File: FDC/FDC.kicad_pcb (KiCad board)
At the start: 2 copper layers, 195.4 x 115.8 mm, 60 parts, among them J1 Bus_ISA_8bit, J2 Floppy IDC, Q1 2N2219, Q2 2N3905, SW1 DSEL, U1 74LS08, U10 74LS161, U11 74LS10, U12 74LS74, U13 74LS08, U14 74LS157, U15 74LS74, U16 74LS175, U17 MC3487N, U18 74LS74, U19 74LS74, U2 74LS32, U20 74LS629, U21 74LS161, U23 74LS175, U24 74LS153, U26 74LS38, U27 74HC240, U3 74LS02, U4 74LS30, U5 74LS245, U6 uPD765BC, U7 74LS04, U8 74LS273, U9 74LS161, X1 16MHZ

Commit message: Large sync
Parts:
- moved C9 178.1 mm to (209.4, 39.1), turned to 180 degrees
- moved C5 168.4 mm to (254.1, 98.3), turned to 90 degrees
- moved C16 151.0 mm to (153.3, 43.8)
- moved C15 139.9 mm to (70.6, 43.7), turned to 270 degrees
- moved C19 136.7 mm to (147.5, 55.1)
- moved C14 126.2 mm to (123.2, 51.3)
- moved C8 119.6 mm to (212.3, 120.9), turned to 270 degrees
- moved C11 75.3 mm to (114.3, 102.4), turned to 270 degrees
- moved C6 74.7 mm to (144.2, 113.9)
- moved C10 61.2 mm to (79.6, 126.5), turned to 270 degrees
- moved C13 59.2 mm to (116.8, 119.0), turned to 90 degrees
- moved C7 55.2 mm to (128.5, 126.7), turned to 270 degrees
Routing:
- net Net-(U26-Pad12): track 10.2 -> 239.3 mm, vias 0 -> 8
- net Net-(U26-Pad10): track 10.2 -> 236.8 mm, vias 0 -> 7
- net /WE: track 53.3 -> 196.0 mm, vias 0 -> 1
- net /TCDACK: track 0.00 -> 123.6 mm, vias 0 -> 2
- net Net-(U26-Pad4): track 0.00 -> 117.5 mm, vias 0 -> 3
- net /TRK0: track 0.00 -> 117.3 mm, vias 0 -> 6
- net Net-(U1-Pad6): track 0.00 -> 80.1 mm, vias 0 -> 3
- net /DMA_GATE: track 54.9 -> 134.2 mm, vias 3 -> 6
- net Net-(U1-Pad10): track 8.67 -> 83.4 mm, vias 0 -> 2
- net +5V: track 174.2 -> 210.1 mm, vias 15 -> 23
- net /TC: track 27.2 -> 59.0 mm, vias 2 -> 1
- net Net-(U3-Pad6): track 52.8 -> 77.4 mm, vias 2 -> 3
- net GND: track 121.4 -> 142.3 mm, vias 4 -> 5
- net /PLL/8MHZ_NOM: track 81.0 -> 79.9 mm
- net Net-(Q2-Pad2): track 13.1 -> 13.8 mm

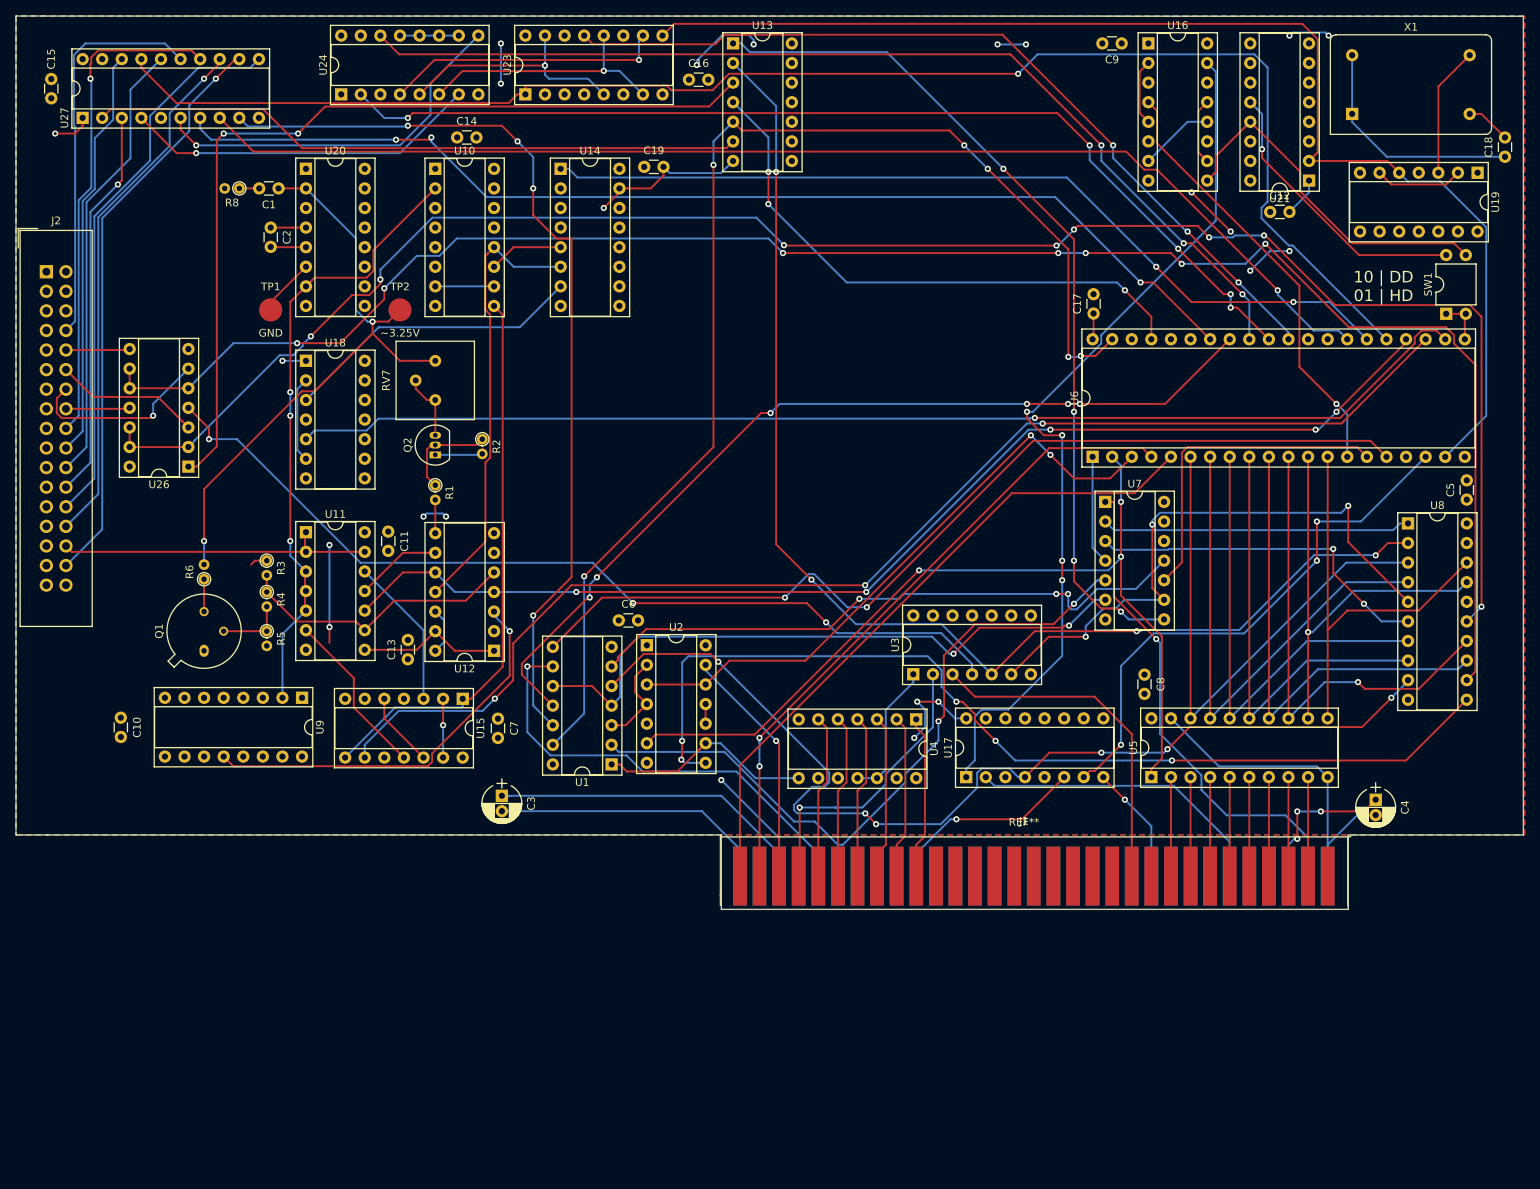
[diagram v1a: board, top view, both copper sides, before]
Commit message: Fixed missing +5V on FDC
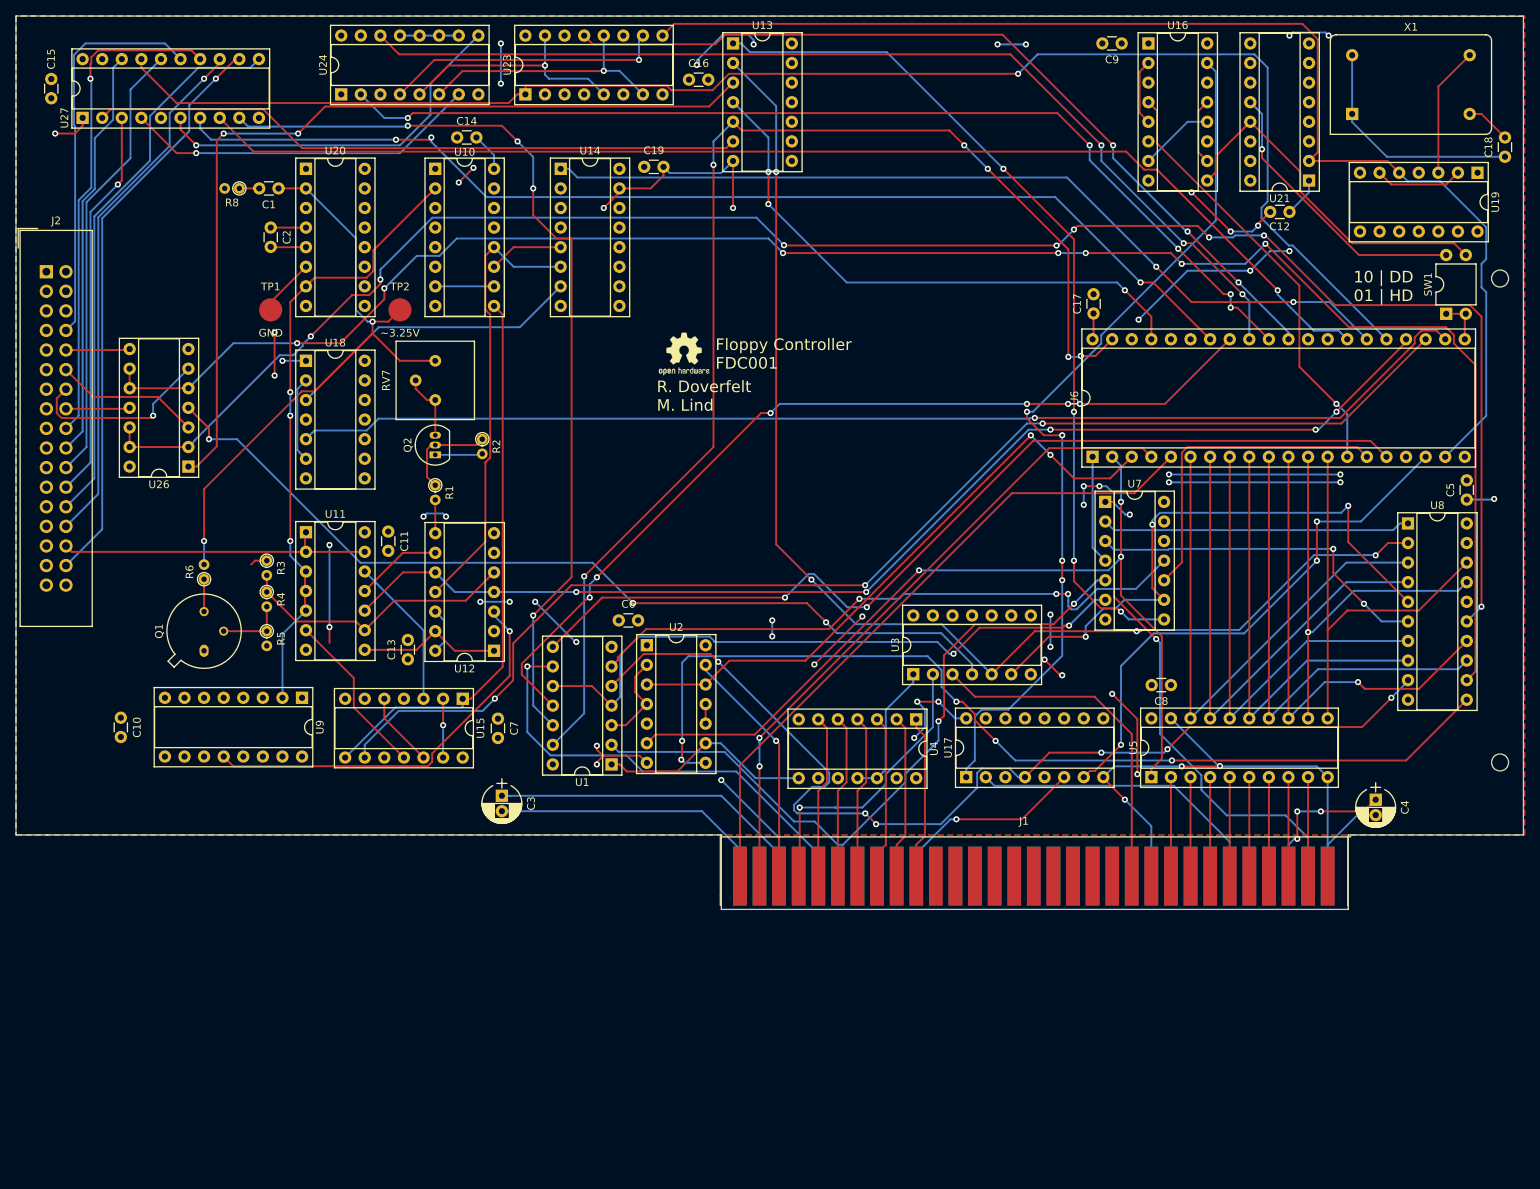
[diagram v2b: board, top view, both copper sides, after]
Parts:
- added REF**: MountingHole_2.2mm_M2_ISO14580, Mounting_Holes:MountingHole_2.2mm_M2_ISO14580, F.Cu at (258.4, 132.3)
- added REF**: MountingHole_2.2mm_M2_ISO14580, Mounting_Holes:MountingHole_2.2mm_M2_ISO14580, F.Cu at (258.4, 69.6)
- added REF***: OSHW-Logo2_7.3x6mm_SilkScreen, Symbols:OSHW-Logo2_7.3x6mm_SilkScreen, F.Cu at (152.7, 79.4)
- moved C8 3.69 mm to (215.8, 122.3), turned to 180 degrees
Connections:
- U23 pad 16: (no net) -> +5V
- U24 pad 16: (no net) -> +5V
- U6 pad 20: GND -> (no net)
- U6 pad 40: +5V -> (no net)
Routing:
- net +5V: track 210.1 -> 308.4 mm, vias 23 -> 41
- net GND: track 142.3 -> 211.6 mm, vias 5 -> 21
- net /8MHZ: track 161.1 -> 161.6 mm
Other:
- board text added: "Floppy Controller FDC001"
- board text added: "R. Doverfelt M. Lind"

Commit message: Work on motherboard  - Integrating glue logic into CPLD  - Began work on routing
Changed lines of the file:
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@@
   (segment (start 106.68 114.788999) (end 106.68 114.514009) (width 0.25) (layer F.Cu) (net 25))
   (segment (start 106.68 114.514009) (end 106.68 116.84) (width 0.25) (layer F.Cu) (net 25))
-  (segment (start 98.552 106.172) (end 97.028 106.172) (width 0.25) (layer F.Cu) (net 25))
-  (segment (start 97.028 106.172) (end 96.52 106.68) (width 0.25) (layer F.Cu) (net 25))
   (segment (start 121.195999 113.575999) (end 120.396 112.776) (width 0.25) (layer B.Cu) (net 25))
   (segment (start 121.521001 113.901001) (end 121.195999 113.575999) (width 0.25) (layer B.Cu) (net 25))
@@
   (via (at 164.084 115.988) (size 0.8) (drill 0.4) (layers F.Cu B.Cu) (net 25))
   (segment (start 164.084 113.919) (end 164.084 115.988) (width 0.25) (layer B.Cu) (net 25))
+  (segment (start 98.552 106.172) (end 97.028 106.172) (width 0.25) (layer F.Cu) (net 25))
+  (segment (start 97.028 106.172) (end 96.774 106.426) (width 0.25) (layer F.Cu) (net 25))
   (via (at 132.334 119.888) (size 0.8) (drill 0.4) (layers F.Cu B.Cu) (net 26))
   (segment (start 132.334 128.411002) (end 132.334 119.888) (width 0.25) (layer B.Cu) (net 26))

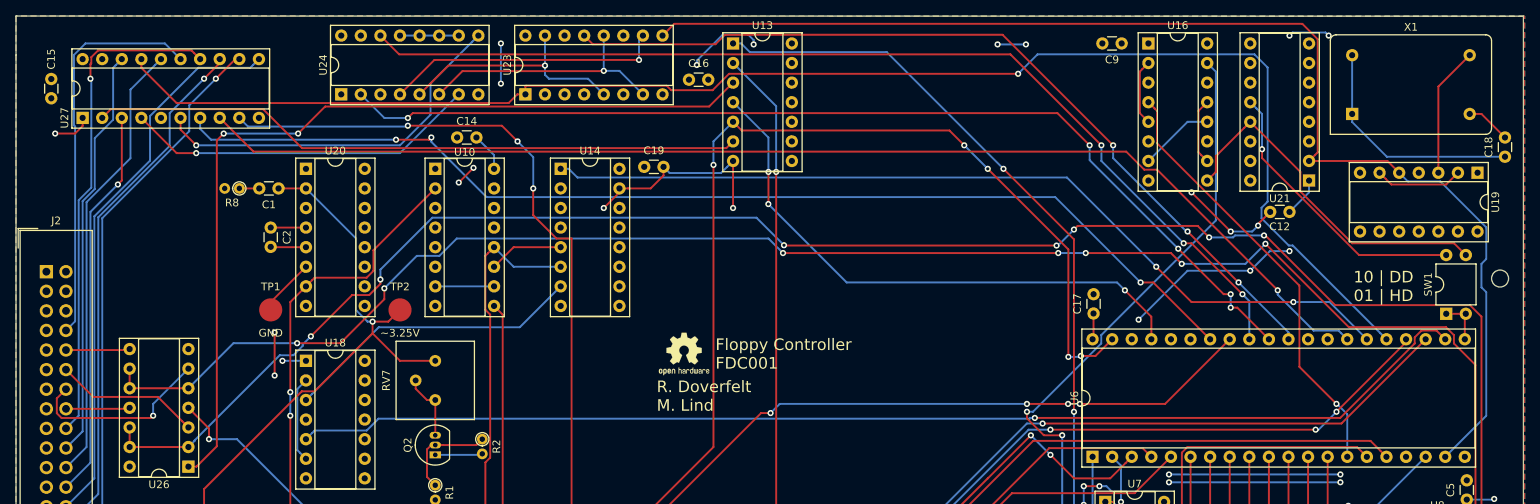
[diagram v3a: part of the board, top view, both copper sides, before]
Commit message: Added missing HD/DD /REDWC option
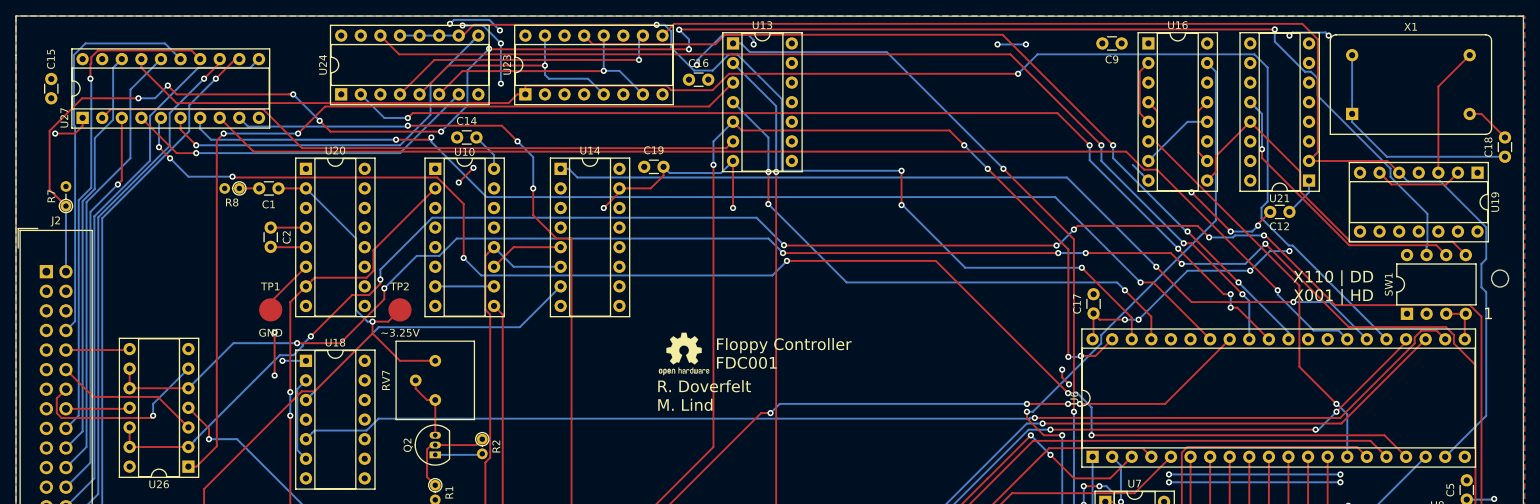
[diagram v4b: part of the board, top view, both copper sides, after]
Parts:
- added R7: 4k7, Resistors_THT:R_Axial_DIN0204_L3.6mm_D1.6mm_P2.54mm_Vertical, F.Cu at (72.5, 60.2)
- SW1: footprint Housings_DIP:DIP-4_W7.62mm -> Housings_DIP:DIP-8_W7.62mm
- moved SW1 5.08 mm to (246.4, 74.2)
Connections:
- J2 pad 2: (no net) -> /~REDWC
- SW1 pad 1: Net-(SW1-Pad1) -> (no net)
- SW1 pad 2: Net-(SW1-Pad1) -> GND
- SW1 pad 3: /2MHZ -> Net-(SW1-Pad3)
- SW1 pad 4: /1MHZ -> Net-(SW1-Pad3)
- U27 pad 5: (no net) -> /INDEX
- U6 pad 17: (no net) -> /INDEX
- U6 pad 20: (no net) -> GND
- U6 pad 21: Net-(SW1-Pad1) -> Net-(SW1-Pad3)
- U6 pad 38: (no net) -> /LCT_DIR
- U6 pad 40: (no net) -> +5V
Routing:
- net /~REDWC: track 0.00 -> 232.3 mm, vias 0 -> 9
- net /INDEX: track 0.00 -> 190.0 mm, vias 0 -> 7
- net /LCT_DIR: track 7.62 -> 125.0 mm, vias 0 -> 4
- net GND: track 211.6 -> 224.0 mm, vias 21 -> 25
- net +5V: track 308.1 -> 320.2 mm, vias 41 -> 43
- net Net-(SW1-Pad3): track 0.00 -> 5.89 mm
- net Net-(SW1-Pad1): track 5.89 -> 0.00 mm
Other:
- board text added: "1"
- board text added: "X110 | DD X001 | HD"
- board text removed: "10 | DD 01 | HD"

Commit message: Large sync
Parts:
- added SW2: DSEL, Housings_DIP:DIP-8_W7.62mm, F.Cu at (136.7, 77.7)
- R1: value R_Small -> 2k2
- R2: value R_Small -> 1k
- R5: value R -> 1k
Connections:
- U10 pad 13: (no net) -> /PLL/2MHZ
- U12 pad 11: /PLL/1MHZ -> /PLL/PLLCLK
- U14 pad 6: /PLL/1MHZ -> /PLL/PLLCLK
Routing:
- net /PLL/PLLCLK: track 0.00 -> 68.3 mm, vias 0 -> 3
- net /PLL/1MHZ: track 58.1 -> 30.0 mm, vias 0 -> 1
- net /PLL/2MHZ: track 0.00 -> 23.4 mm
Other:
- board text added: "10XX | DD 01XX | HD"
